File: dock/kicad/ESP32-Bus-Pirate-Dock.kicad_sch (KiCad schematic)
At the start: 18 parts, among them CN1 HX25418-10WA, J1 Conn_01x22, J2 Conn_01x22, J3 Conn_01x10V, J4 Conn_01x22, J5 Conn_01x22, J6 Conn_01x22, J7 Conn_02x03, U1 ESP32-S3-DEVKITC-1-N8R2, U2 TLV75518PDBV

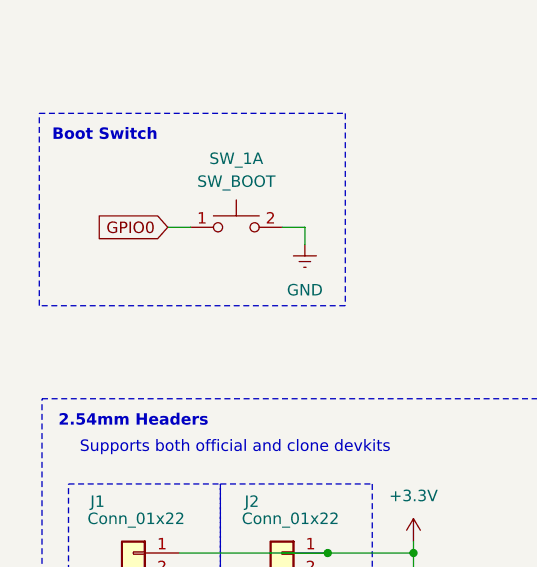
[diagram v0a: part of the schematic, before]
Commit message: Added LCSC Parts & Board Version to v3
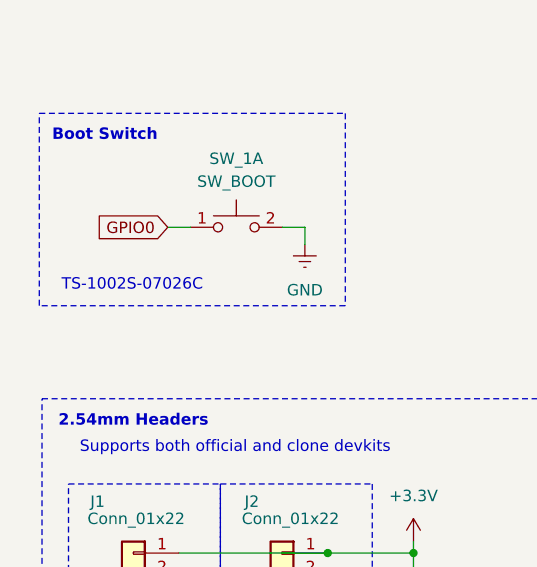
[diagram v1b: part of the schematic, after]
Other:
- note added: "TS-1002S-07026C"
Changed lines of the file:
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@@
+		)
+	)
+	(text "TS-1002S-07026C"
+		(exclude_from_sim no)
+		(at 32.258 98.552 0)
+		(effects
+			(font
+				(size 1.27 1.27)
+				(color 132 132 0 1)
+			)
 		)
 	)

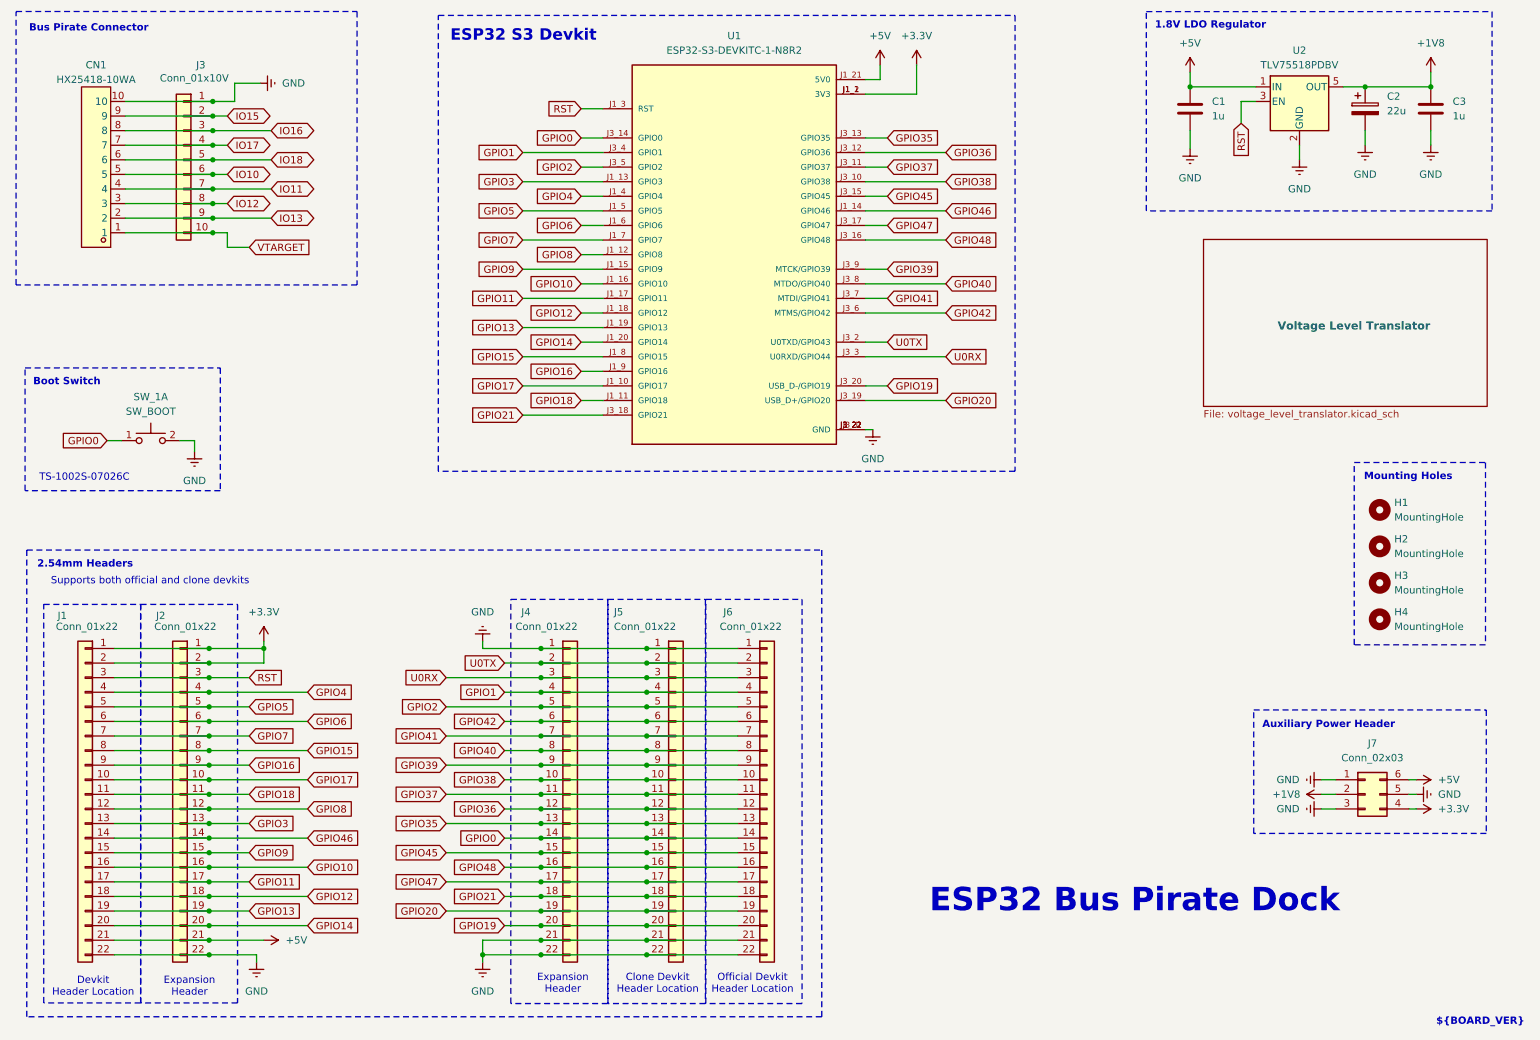
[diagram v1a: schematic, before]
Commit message: Added testpoints, J3 mirrored
- J3 mirrored in order to share the same pin numbers with CN1. It just makes it less confusing.

- Added test points on power supplies, and SEL signals just to help test the board.
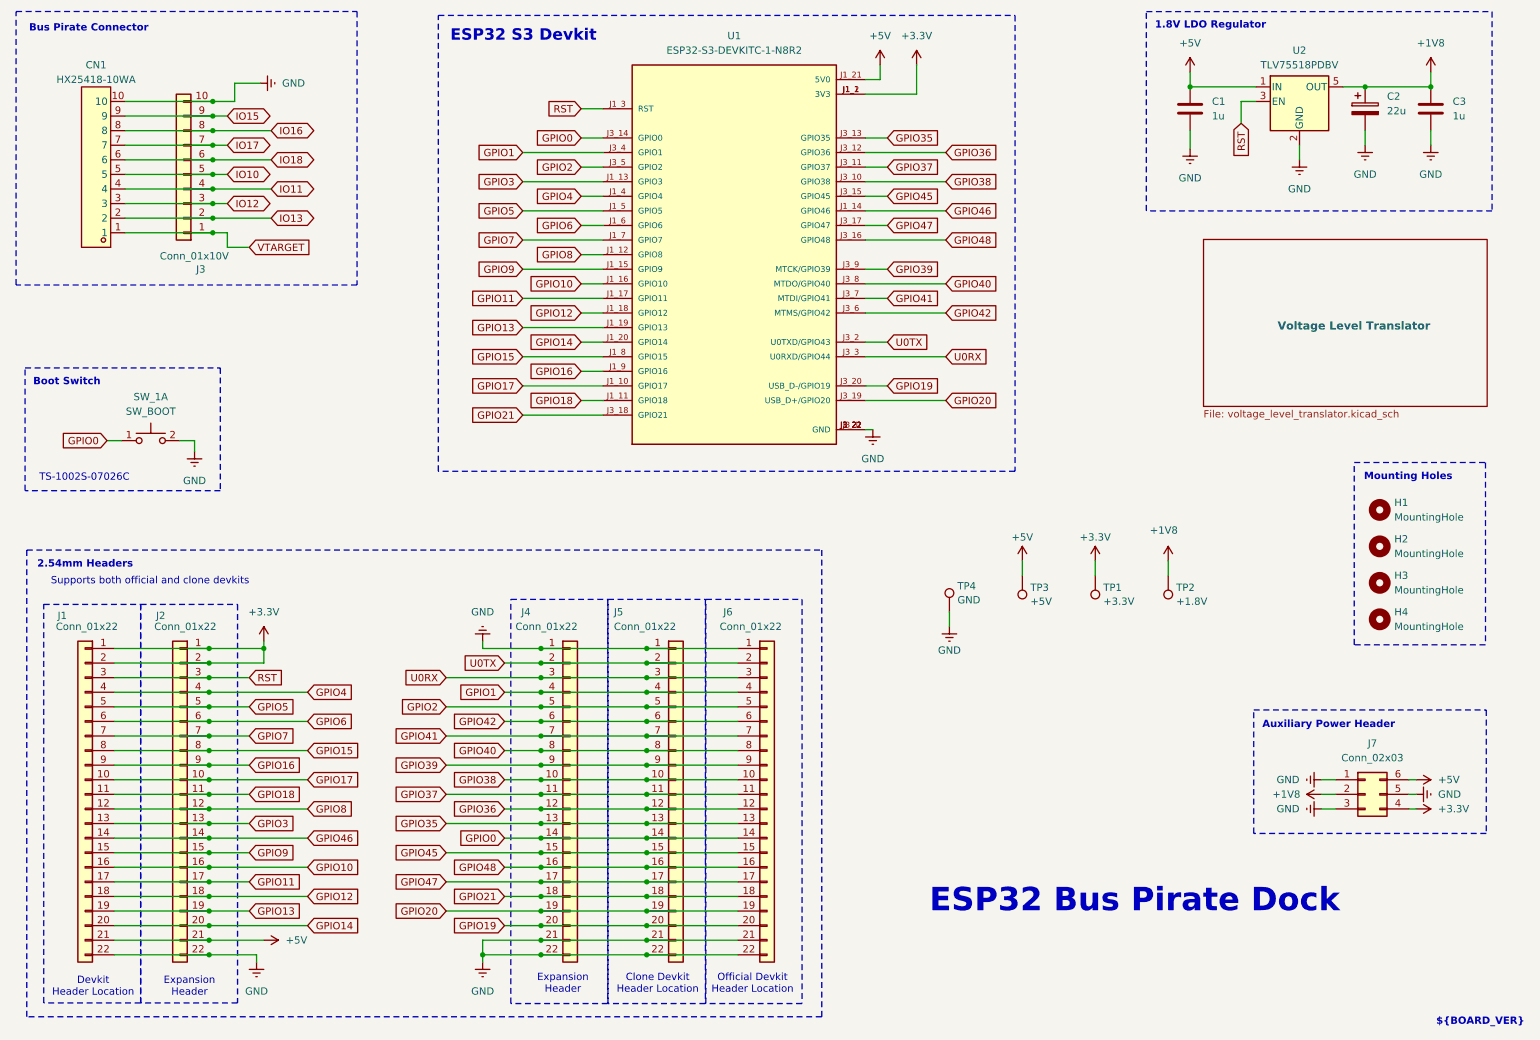
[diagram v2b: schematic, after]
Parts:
- added TP1: +3.3V, TestPoint:TestPoint_Pad_D1.0mm, symbol Connector:TestPoint
- added TP2: +1.8V, TestPoint:TestPoint_Pad_D1.0mm, symbol Connector:TestPoint
- added TP3: +5V, TestPoint:TestPoint_Pad_D1.0mm, symbol Connector:TestPoint
- added TP4: GND, TestPoint:TestPoint_Pad_D1.0mm, symbol Connector:TestPoint
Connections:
- net +1V8: now also TP2.1
- net +3.3V: now also TP1.1
- net +5V: now also TP3.1
- net GND: now also J3.10 (Pin_10), TP4.1; no longer J3.1 (Pin_1)
- net IO10: now also J3.5 (Pin_5); no longer J3.6 (Pin_6)
- net IO11: now also J3.4 (Pin_4); no longer J3.7 (Pin_7)
- net IO12: now also J3.3 (Pin_3); no longer J3.8 (Pin_8)
- net IO13: now also J3.2 (Pin_2); no longer J3.9 (Pin_9)
- net IO15: now also J3.9 (Pin_9); no longer J3.2 (Pin_2)
- net IO16: now also J3.8 (Pin_8); no longer J3.3 (Pin_3)
- net IO17: now also J3.7 (Pin_7); no longer J3.4 (Pin_4)
- net IO18: now also J3.6 (Pin_6); no longer J3.5 (Pin_5)
- net VTARGET: now also J3.1 (Pin_1); no longer J3.10 (Pin_10)
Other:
- moved on the sheet: J3

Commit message: Modified test pads & added TC2050
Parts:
- removed TP1: +3.3V, TestPoint:TestPoint_Pad_D1.0mm, symbol Connector:TestPoint
- removed TP2: +1.8V, TestPoint:TestPoint_Pad_D1.0mm, symbol Connector:TestPoint
- removed TP3: +5V, TestPoint:TestPoint_Pad_D1.0mm, symbol Connector:TestPoint
- removed TP4: GND, TestPoint:TestPoint_Pad_D1.0mm, symbol Connector:TestPoint

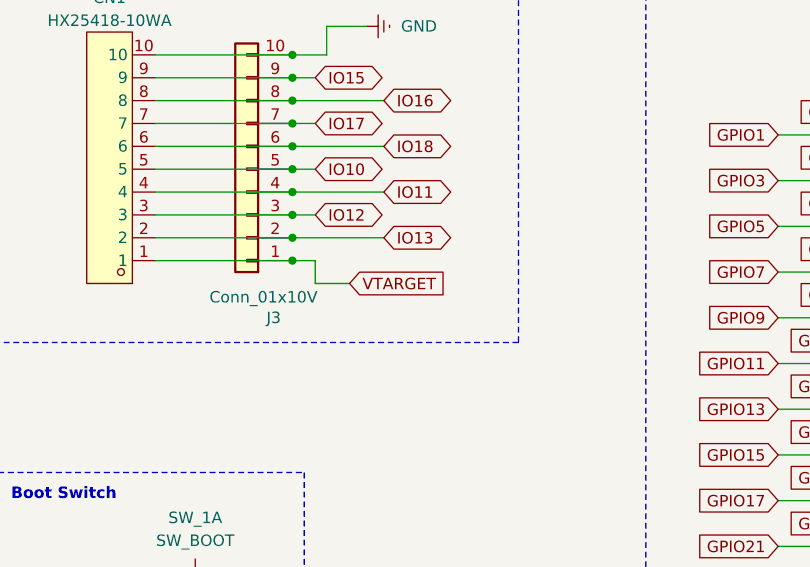
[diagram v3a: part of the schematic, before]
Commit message: Changed VTarget to Vio
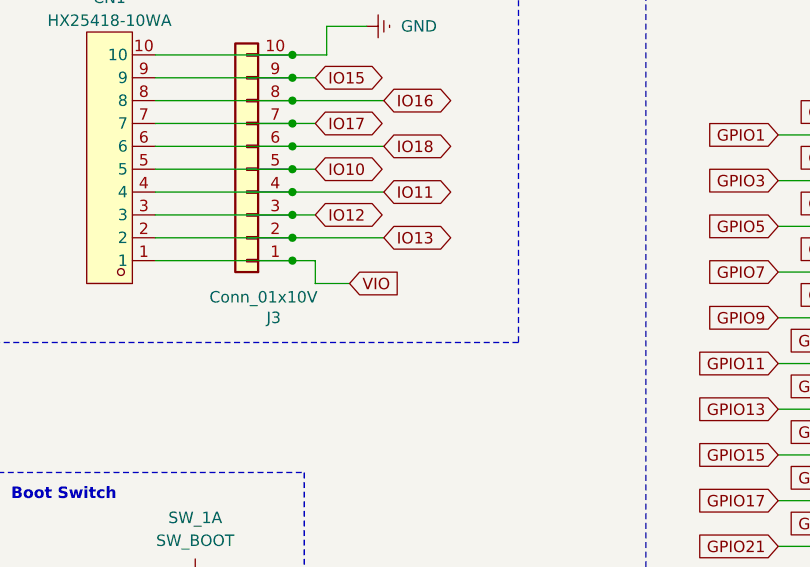
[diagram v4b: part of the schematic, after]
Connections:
- net VTARGET renamed VIO
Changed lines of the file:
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@@
 		)
 	)
-	(global_label "VTARGET"
+	(global_label "VIO"
 		(shape input)
 		(at 60.96 58.42 0)
@@
 		)
 		(property "Intersheetrefs" "${INTERSHEET_REFS}"
-			(at 71.7466 58.42 0)
+			(at 66.9691 58.42 0)
 			(effects
 				(font

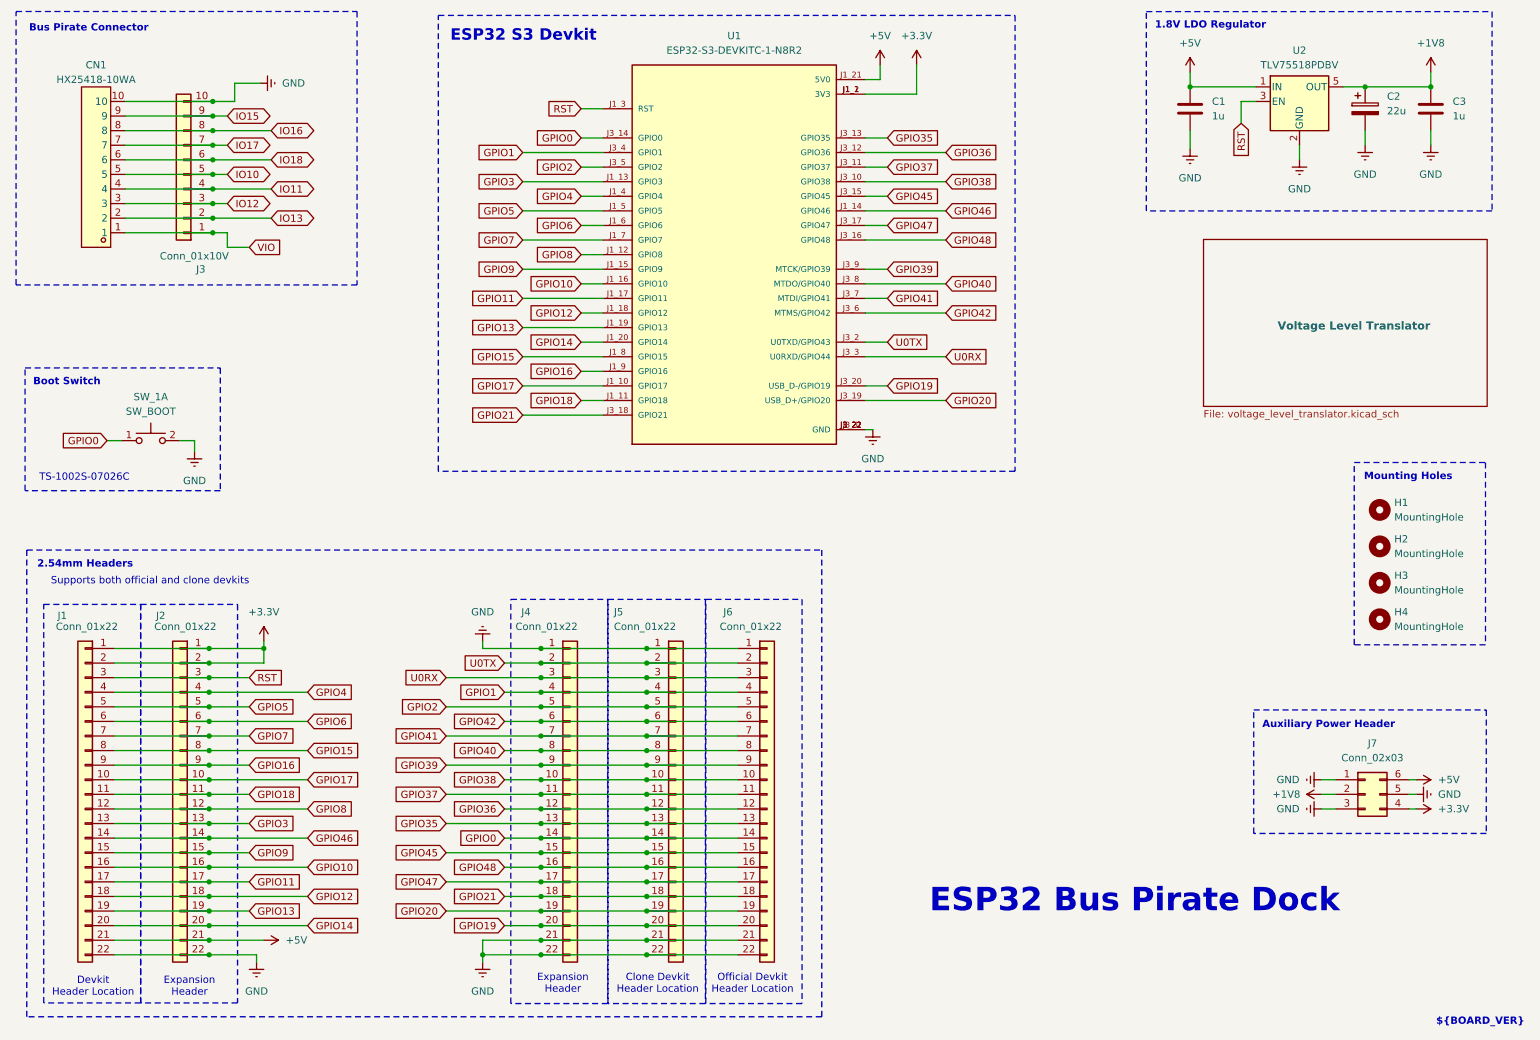
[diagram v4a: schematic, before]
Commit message: Minor schematic changes
- Added net classes
- Added cosmetic changes
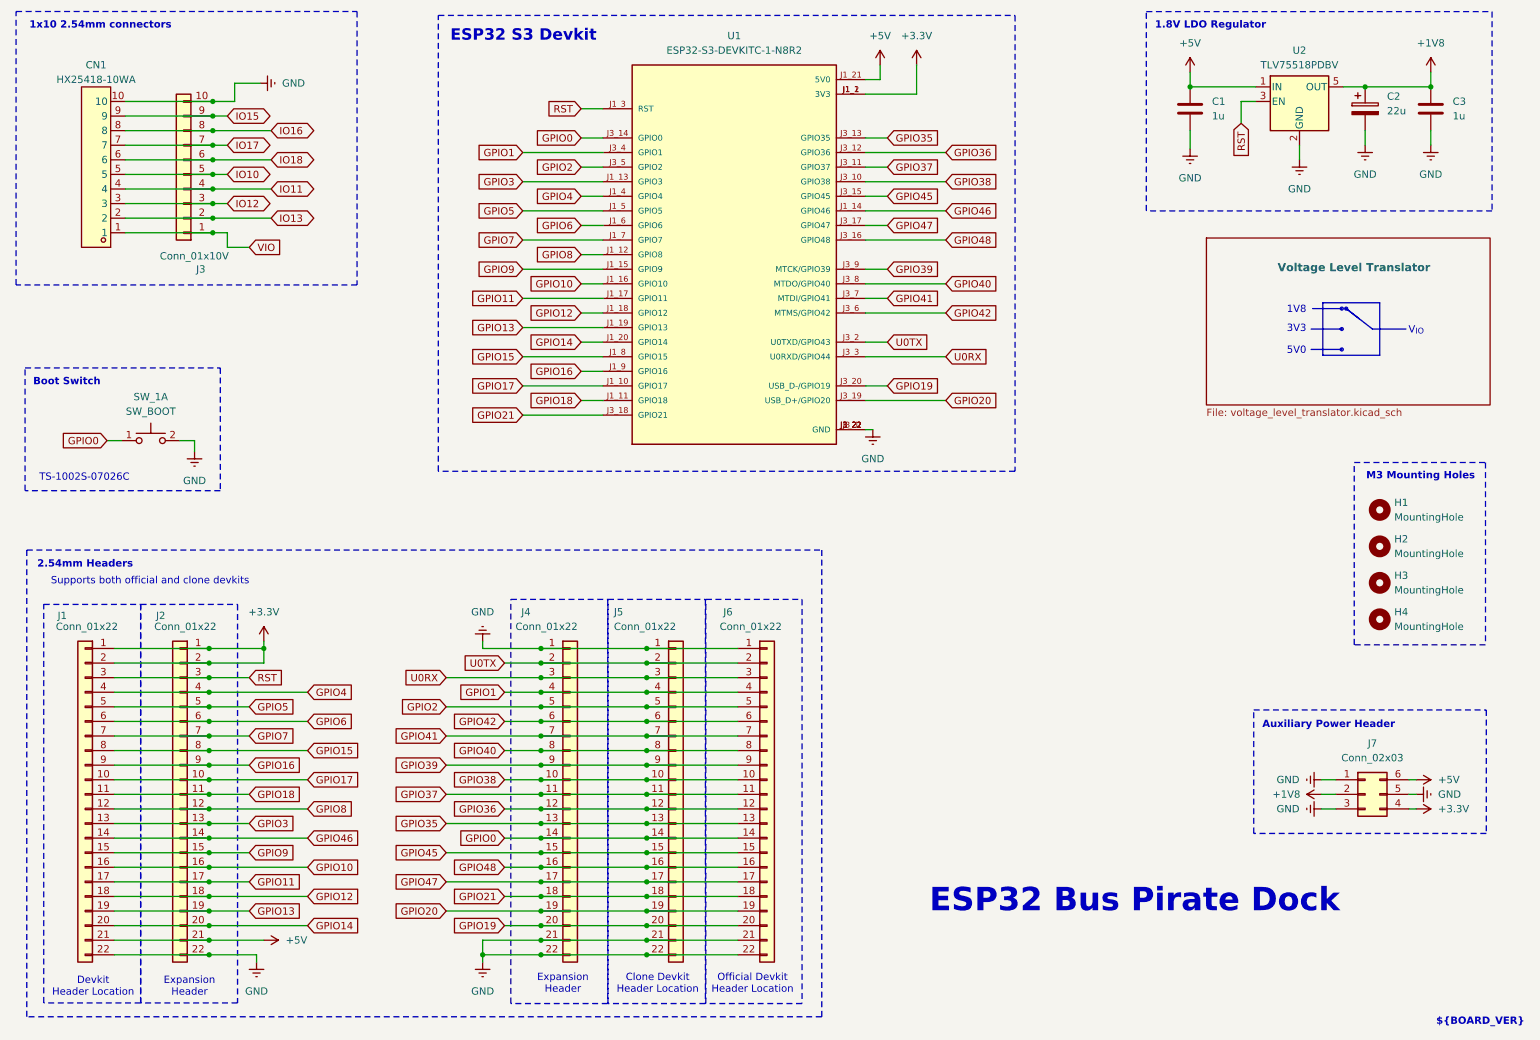
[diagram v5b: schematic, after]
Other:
- note added: "1V8"
- note added: "1x10 2.54mm connectors"
- note added: "3V3"
- note added: "5V0"
- note added: "M3 Mounting Holes"
- note added: "V_{IO}"
- note removed: "Bus Pirate Connector"
- note removed: "Mounting Holes"
